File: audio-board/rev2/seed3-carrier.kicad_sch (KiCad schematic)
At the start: 86 parts, among them J1 AudioJack2_Switch, J2 AudioJack2, J3 POWER_BOARD, J4 DISPLAY_UART, J5 SJ3-35063AG, J6 Seed3_PINS_RIGHT, J7 Seed3_PINS_LEFT, J8 LINE_OUT, J9 SJ3-35063AG, Q1 AO3401A, Q3 2N7002, Q4 2N7002, SW1 EC11E, U1 TLV9064IDR, U2 TPA6132A2RTE, U3 SN74LVC1G123DCTR

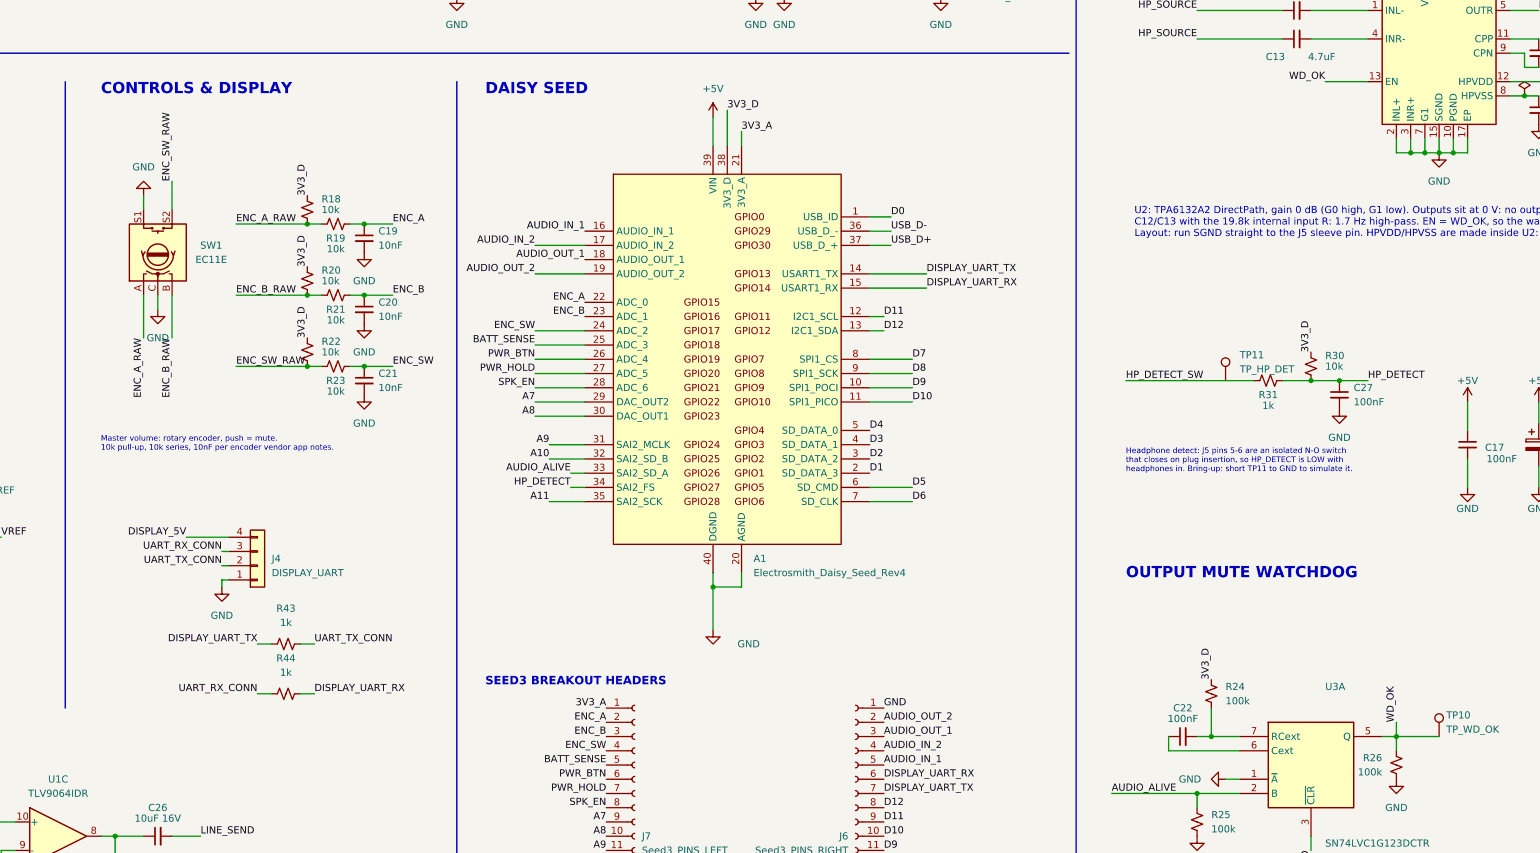
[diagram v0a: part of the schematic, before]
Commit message: Rev 2 schematic: remove encoder, set revision 2.0
Remove the master volume encoder (SW1, R18-R23, C19-C21). Volume moves
to the touchscreen/ESP32 side. Daisy pins 22-24 are now spare and go
only to the J7 breakout as A0-A2. Set the schematic revision to 2.0 and
update CHANGES.md to match. ERC: 0 violations.

Co-Authored-By: Claude Opus 5.5 <noreply@anthropic.com>
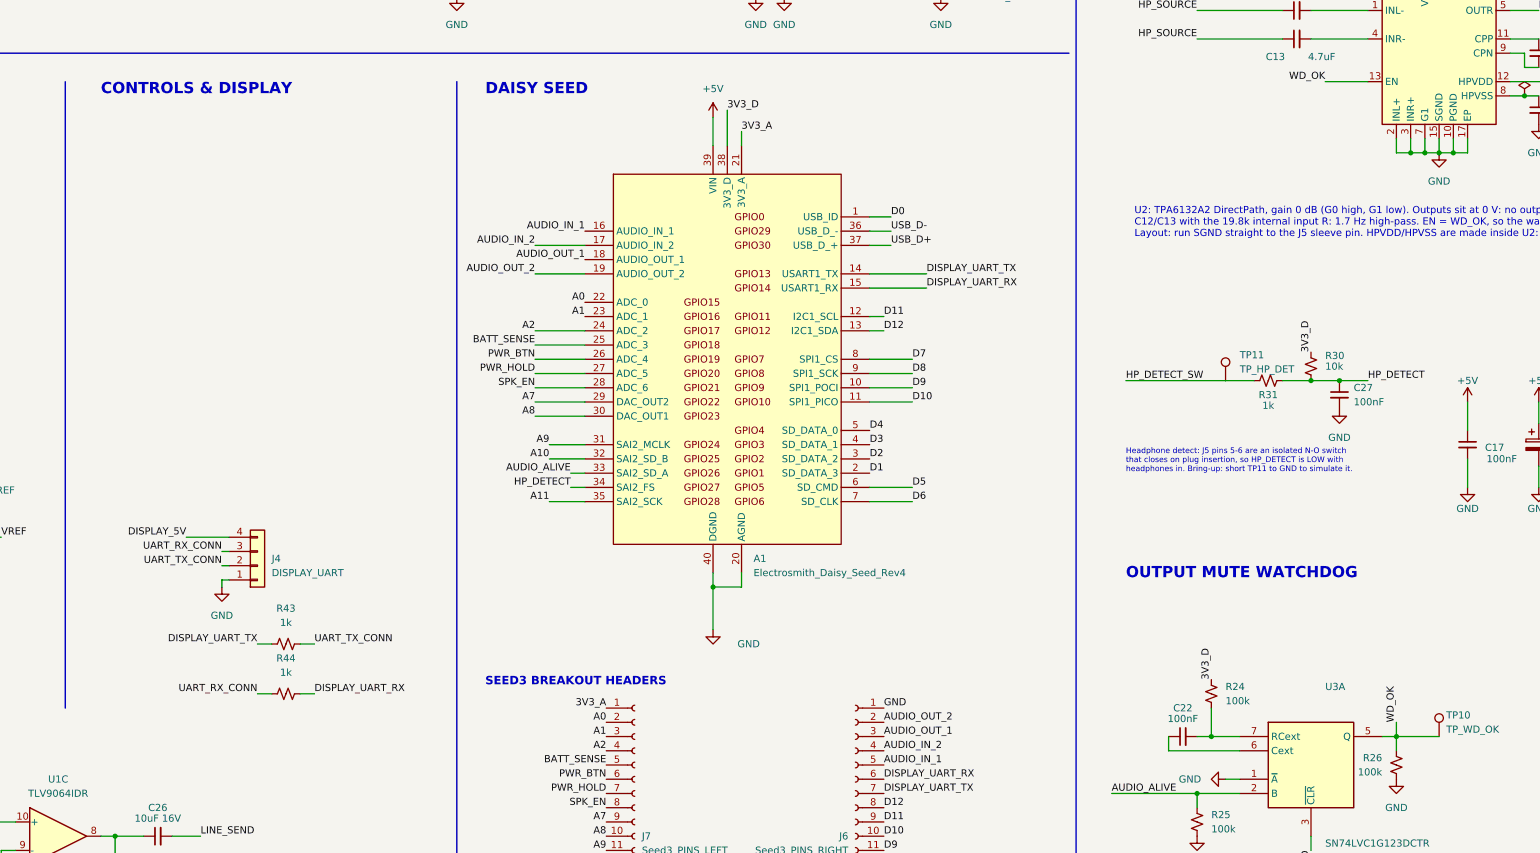
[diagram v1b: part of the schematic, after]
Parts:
- removed C19, C20, C21: 10nF, Capacitor_SMD:C_1206_3216Metric_Pad1.33x1.80mm_HandSolder, symbol Device:C_Small
- removed R18, R19, R20, R21, R22, R23: 10k, Resistor_SMD:R_1206_3216Metric_Pad1.30x1.75mm_HandSolder, symbol Device:R_Small_US
- removed SW1: EC11E, Rotary_Encoder:RotaryEncoder_Alps_EC11E-Switch_Vertical_H20mm, symbol Device:RotaryEncoder_Switch
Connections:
- net ENC_A renamed A0
- net ENC_B renamed A1
- net ENC_SW renamed A2
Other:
- note removed: "Master volume: rotary encoder, push = mute. 10k pull-up, 10k series, 10nF per encoder vendor app notes."

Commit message: Rev 2: replace U3 watchdog with STM32 IWDG
Remove U3 (SN74LVC1G123), R24, R25, C22, C23 and Q3. Daisy pin 33
(HP_EN, was AUDIO_ALIVE) drives U2 EN directly with R26 pull-down,
and Q4 alone drives SPK_MUTE from SPK_EN. Firmware feeds the internal
watchdog only from the audio callback; on reset the pins float and
the pull-downs mute both amps. TP10 renamed TP_HP_EN.

Co-Authored-By: Claude Opus 5.5 <noreply@anthropic.com>
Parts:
- removed C22, C23: 100nF, Capacitor_SMD:C_1206_3216Metric_Pad1.33x1.80mm_HandSolder, symbol Device:C_Small
- removed Q3: 2N7002, Package_TO_SOT_SMD:SOT-23, symbol Transistor_FET:2N7002
- removed R24, R25: 100k, Resistor_SMD:R_1206_3216Metric_Pad1.30x1.75mm_HandSolder, symbol Device:R_Small_US
- removed U3: SN74LVC1G123DCTR, Package_SO:SSOP-8_2.95x2.8mm_P0.65mm, symbol 74xGxx:74LVC1G123
- TP10: value TP_WD_OK -> TP_HP_EN
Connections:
- net WD_OK is gone; now on net HP_EN: R26.1, TP10.1, U2.13 (EN)
- net SPK_MUTE: now also Q4.3 (D)
- net AUDIO_ALIVE renamed HP_EN
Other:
- note added: "HP_EN (Daisy pin 33) drives U2 EN directly. R26 holds it low, so U2 stays off while the Daisy is absent, booting, in DFU or being reset. The firmware feeds the STM32 internal watchdog (IWDG) only from the audio callback: if audio stops, the STM32 resets, its pins float, and R26 (U2) and R37 (Q4, speaker) mute both amps. The speaker amp mute is SPK_MUTE on J3."
- note added: "J3 goes to the power board (JST-XH, 8 pins). Pins 5-7 are 3.3 V logic: nothing above 3.3 V on them. SPK_MUTE is open drain. The power board pulls it up, so the speaker amp stays muted unless SPK_EN is high."
- note added: "OUTPUT MUTE"
- note added: "U2: TPA6132A2 DirectPath, gain 0 dB (G0 high, G1 low). Outputs sit at 0 V: no output caps. C12/C13 with the 19.8k internal input R: 1.7 Hz high-pass. EN = HP_EN, pulled low by R26. Layout: run SGND straight to the J5 sleeve pin. HPVDD/HPVSS are made inside U2: caps only."
- note removed: "J3 goes to the power board (JST-XH, 8 pins). Pins 5-7 are 3.3 V logic: nothing above 3.3 V on them. SPK_MUTE is open drain. The power board pulls it up, so the speaker amp stays muted unless WD_OK and SPK_EN are both high."
- note removed: "OUTPUT MUTE WATCHDOG"
- note removed: "U2 stays off (EN = WD_OK low) unless the firmware toggles AUDIO_ALIVE from the audio callback. Each rising edge retriggers U3; if edges stop for ~10 ms (Rext x Cext), Q (WD_OK) falls: U2 shuts down and Q3 mutes the speaker amp. Also muted while the Daisy is absent, booting or in DFU (B is held low). The speaker amp mute is SPK_MUTE on J3."
- note removed: "U2: TPA6132A2 DirectPath, gain 0 dB (G0 high, G1 low). Outputs sit at 0 V: no output caps. C12/C13 with the 19.8k internal input R: 1.7 Hz high-pass. EN = WD_OK, so the watchdog shuts U2 down. Layout: run SGND straight to the J5 sleeve pin. HPVDD/HPVSS are made inside U2: caps only."

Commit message: Use 0.3 mm vias under U2 and set board design rules
U2 footprint:
- Switch to WQFN-16-1EP_3x3mm_P0.5mm_EP1.6x1.6mm (no thermal vias) in the
  schematic and symbol library; the _ThermalVias variant drills 0.2 mm,
  below the 0.3 mm minimum hole
- Add four 0.6/0.3 mm GND vias in the exposed pad on the board

Design rules:
- Minimum track width 0.3 -> 0.2 mm (matched the Default class, which
  failed DRC), minimum annular ring 0.1 -> 0.15 mm
- New Power net class (1 mm track, 0.8/0.4 via) for +5V, 5V_IN,
  DISPLAY_5V, 3V3_A and 3V3_D; track and via presets
- seed3-carrier.kicad_dru adds per-class min/opt/max for track width and
  via size

DRC: no violations beyond unrouted nets and front-edge silkscreen;
0 schematic parity issues. CHANGES.md records both changes.

Co-Authored-By: Claude Opus 5.5 <noreply@anthropic.com>
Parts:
- U2: footprint Package_DFN_QFN:WQFN-16-1EP_3x3mm_P0.5mm_EP1.6x1.6mm_ThermalVias -> Package_DFN_QFN:WQFN-16-1EP_3x3mm_P0.5mm_EP1.6x1.6mm
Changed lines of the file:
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@@
 			)
 		)
-		(property "Footprint" "Package_DFN_QFN:WQFN-16-1EP_3x3mm_P0.5mm_EP1.6x1.6mm_ThermalVias"
+		(property "Footprint" "Package_DFN_QFN:WQFN-16-1EP_3x3mm_P0.5mm_EP1.6x1.6mm"
 			(at 345.44 63.5 0)
 			(hide yes)

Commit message: Add LCSC part numbers to the carrier board BOM
- Hidden LCSC field on every schematic symbol except the Neutrik
  jacks (not stocked at LCSC); copied to the board footprints so
  schematic parity stays clean
- Parts chosen from JLC's library on 2026-10-25: 11 basic and 11
  extended SMD lines for JLC assembly, plus LCSC numbers for the
  hand-soldered through-hole parts
- C0G kept for the RC filter caps; 3 A ferrite bead for the display
  feed; C7, C18 and C9/C26 use higher-voltage parts in the same
  footprints
- CHANGES.md: parts table with stock, and an open item for U2
  (TPA6132A2RTER, only 65 at JLC)

ERC clean; DRC shows only unrouted nets and front-edge jack
silkscreen; 0 schematic parity issues.

Co-Authored-By: Claude Opus 5.5 <noreply@anthropic.com>
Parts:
- C1: LCSC (none) -> C107179
- C12, C13: LCSC (none) -> C86052
- C17, C27, C28, C29, C8: LCSC (none) -> C24497
- C18: LCSC (none) -> C2835642
- C2, C24, C31: LCSC (none) -> C1885
- C25, C3, C32, C5: LCSC (none) -> C1848
- C26, C9: LCSC (none) -> C13585
- C30, C7: LCSC (none) -> C77101
- C33, C34, C36: LCSC (none) -> C19110
- C35: LCSC (none) -> C28323
- FB1: LCSC (none) -> C357023
- J3: LCSC (none) -> C157972
- J4: LCSC (none) -> C53055674
- J5, J9: LCSC (none) -> C39461671
- J6, J7: LCSC (none) -> C2905423
- J8: LCSC (none) -> C158012
- Q1: LCSC (none) -> C15127
- Q4: LCSC (none) -> C8545
- R1, R31, R33, R35, R42, R43, R44: LCSC (none) -> C4410
- R17, R29, R6: LCSC (none) -> C17927
- R2, R28: LCSC (none) -> C26032
- R26, R34, R37, R39, R4: LCSC (none) -> C17900
- R3: LCSC (none) -> C17901
- R30, R32, R36, R40, R41, R7, R8: LCSC (none) -> C17902
- R38: LCSC (none) -> C25833
- R5: LCSC (none) -> C26119
- U1: LCSC (none) -> C388176
- U2: LCSC (none) -> C69901

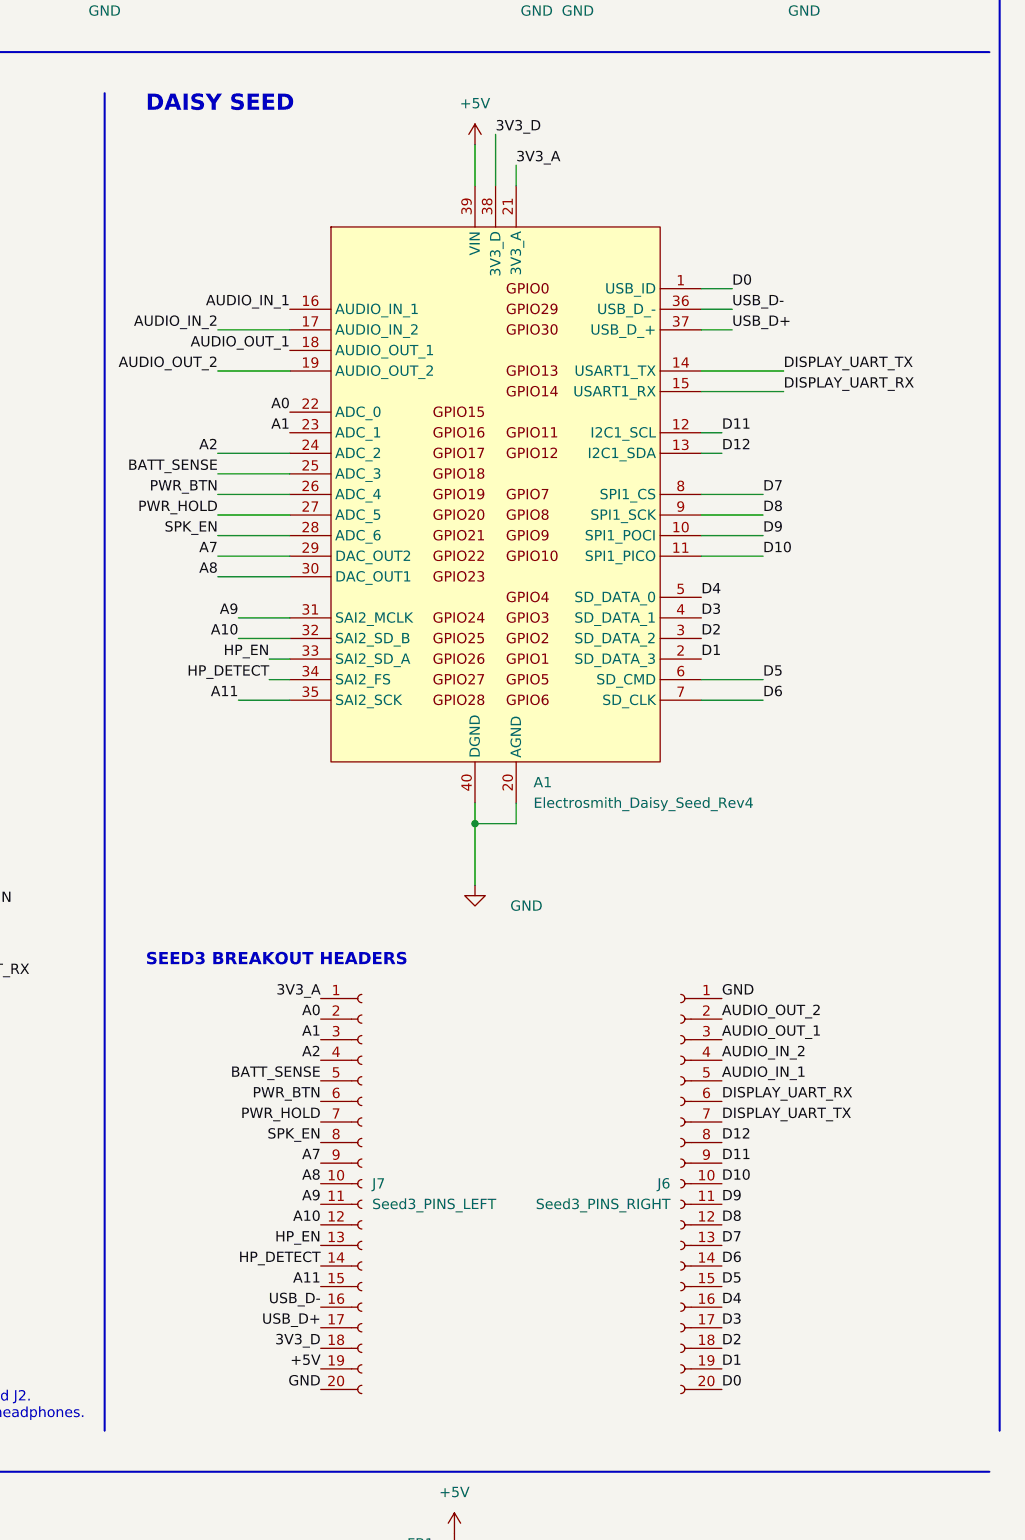
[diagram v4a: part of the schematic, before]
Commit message: Remove J6/J7 breakouts and shrink board to 90 x 56.5 mm
Schematic:
- J6/J7 (1x20 sockets mirroring the Daisy), their 40 labels and the
  breakout heading removed
- The 24 Daisy pins that only went to them (D0-D12, A0-A2, A7-A11,
  USB D+/D-, 3V3_A) marked no-connect; ERC clean

Board:
- J6/J7 footprints removed; Daisy pads synced to the new nets
- Daisy moved 5.4 mm into J7's strip; jacks and analog section moved
  5.5 mm with it. 90 x 62 -> 90 x 56.5 mm
- Display group repacked beside J4 on the right edge; spacing (>= 1 mm
  between different-net pads) kept apart from the deliberate U1/U2 cases
- Zones refilled, labels re-placed

Docs:
- TEST_PLAN.md probes the Daisy sockets (A1.n) with the module out, or a
  carrier part on the same net with it fitted; breakout check removed
- CHANGES.md: removal, new outline, placement notes

DRC: only unrouted nets and front-edge jack silkscreen; 0 schematic
parity issues.

Co-Authored-By: Claude Opus 5.5 <noreply@anthropic.com>
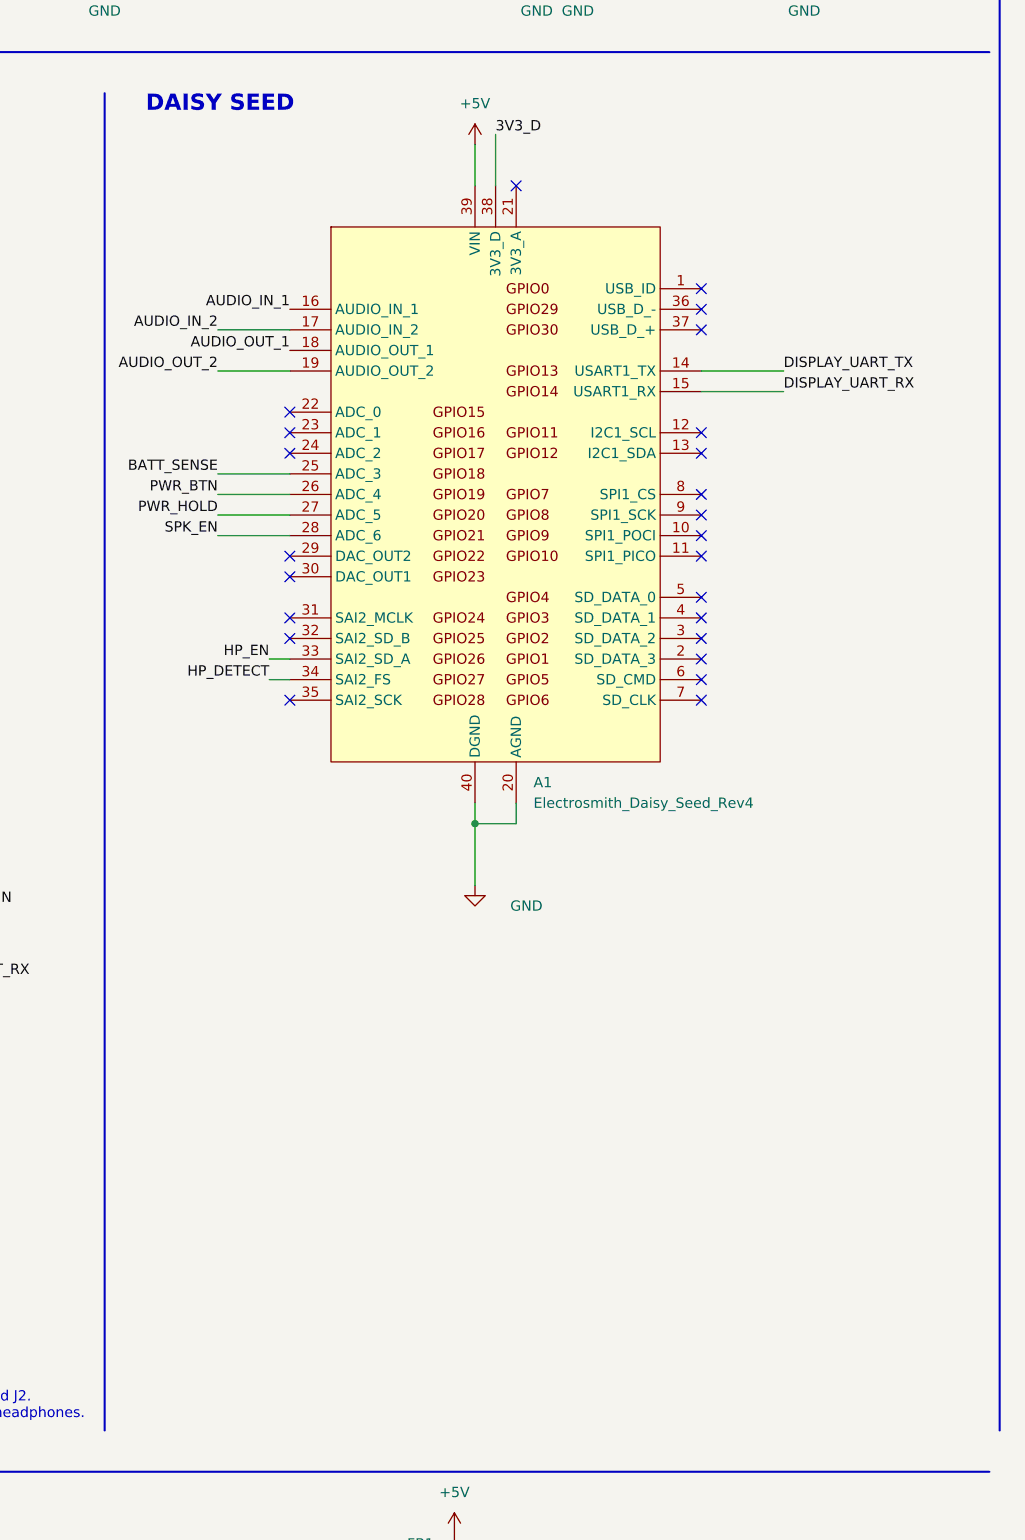
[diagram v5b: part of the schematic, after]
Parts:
- removed J6: Seed3_PINS_RIGHT, Connector_PinSocket_2.54mm:PinSocket_1x20_P2.54mm_Vertical, symbol Connector:Conn_01x20_Socket
- removed J7: Seed3_PINS_LEFT, Connector_PinSocket_2.54mm:PinSocket_1x20_P2.54mm_Vertical, symbol Connector:Conn_01x20_Socket
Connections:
- net 3V3_A: no longer names the net of A1.21 (3V3_A)
- net A0: no longer names the net of A1.22 (ADC_0)
- net A1: no longer names the net of A1.23 (ADC_1)
- net A10: no longer names the net of A1.32 (SAI2_SD_B)
- net A11: no longer names the net of A1.35 (SAI2_SCK)
- net A2: no longer names the net of A1.24 (ADC_2)
- net A7: no longer names the net of A1.29 (DAC_OUT2)
- net A8: no longer names the net of A1.30 (DAC_OUT1)
- net A9: no longer names the net of A1.31 (SAI2_MCLK)
- net D0: no longer names the net of A1.1 (USB_ID)
- net D1: no longer names the net of A1.2 (SD_DATA_3)
- net D10: no longer names the net of A1.11 (SPI1_PICO)
- net D11: no longer names the net of A1.12 (I2C1_SCL)
- net D12: no longer names the net of A1.13 (I2C1_SDA)
- net D2: no longer names the net of A1.3 (SD_DATA_2)
- net D3: no longer names the net of A1.4 (SD_DATA_1)
- net D4: no longer names the net of A1.5 (SD_DATA_0)
- net D5: no longer names the net of A1.6 (SD_CMD)
- net D6: no longer names the net of A1.7 (SD_CLK)
- net D7: no longer names the net of A1.8 (SPI1_CS)
- net D8: no longer names the net of A1.9 (SPI1_SCK)
- net D9: no longer names the net of A1.10 (SPI1_POCI)
- net USB_D+: no longer names the net of A1.37 (USB_D_+)
- net USB_D-: no longer names the net of A1.36 (USB_D_-)
- no-connect marks 3 -> 27
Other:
- note removed: "SEED3 BREAKOUT HEADERS"

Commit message: Remove TP5/TP9/TP10, C9 and the U1B headphone buffer
TP5, TP9 and TP10 duplicated pads that are easy to probe (C7, C18,
R26), and C9 sat on the same node as C18 and C17. The test plan now
probes those parts instead.

The Seed3's AC-coupled 1 Vrms outputs can drive U2's ~9.9 kOhm input
load through R2, as Electrosmith's own reference circuits do, so C5 and
R6 are gone. HP_SOURCE is now the R2/C2 node, and U1B is parked as a
VREF follower. Full scale reaches U2 at about 0.75 Vrms, below its
clip point.

Co-Authored-By: Claude Opus 5.5 <noreply@anthropic.com>
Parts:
- removed C5: 1uF, Capacitor_SMD:C_1206_3216Metric_Pad1.33x1.80mm_HandSolder, symbol Device:C_Small
- removed C9: 10uF 16V, Capacitor_SMD:C_1206_3216Metric_Pad1.33x1.80mm_HandSolder, symbol Device:C_Small
- removed R6: 1M, Resistor_SMD:R_1206_3216Metric_Pad1.30x1.75mm_HandSolder, symbol Device:R_Small_US
- removed TP10: TP_HP_EN, TestPoint:TestPoint_Pad_D2.0mm, symbol Connector:TestPoint
- removed TP5: TP_VREF, TestPoint:TestPoint_Pad_D2.0mm, symbol Connector:TestPoint
- removed TP9: TP_5V, TestPoint:TestPoint_Pad_D2.0mm, symbol Connector:TestPoint
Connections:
- net HP_SOURCE: now also C2.1, R2.1; no longer U1.6 (-), U1.7
- net VREF: now also U1.5 (+)
- new net: U1.6 (-), U1.7
